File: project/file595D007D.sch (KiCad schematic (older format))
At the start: 8 parts

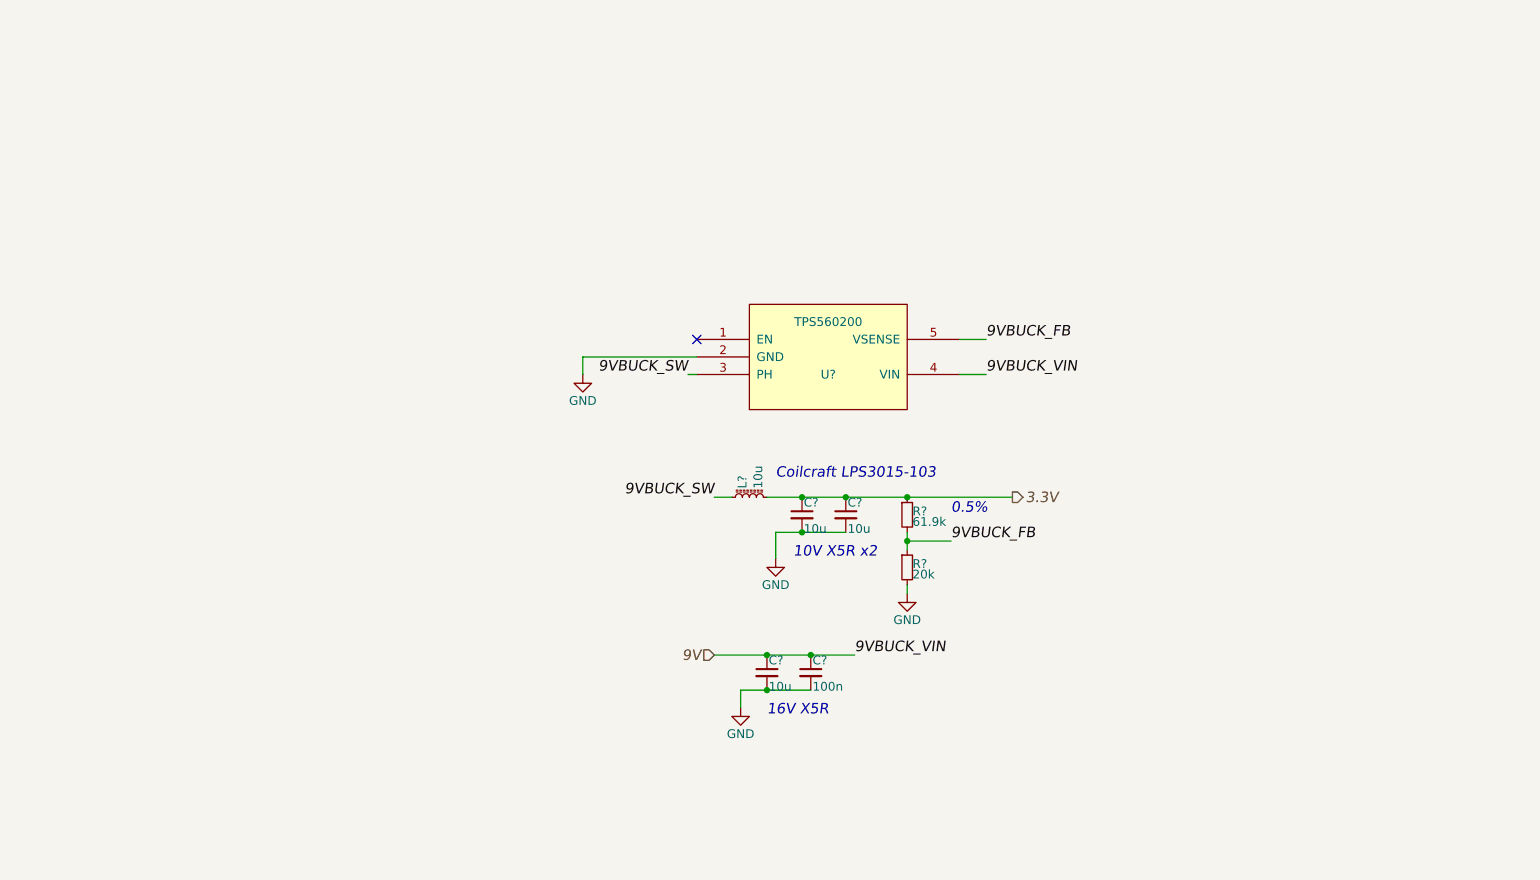
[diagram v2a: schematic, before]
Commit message: Update README with links to documentation for all parts entered in schematic so far. Add 9V to 14V boost converter for output amplifier to schematic.
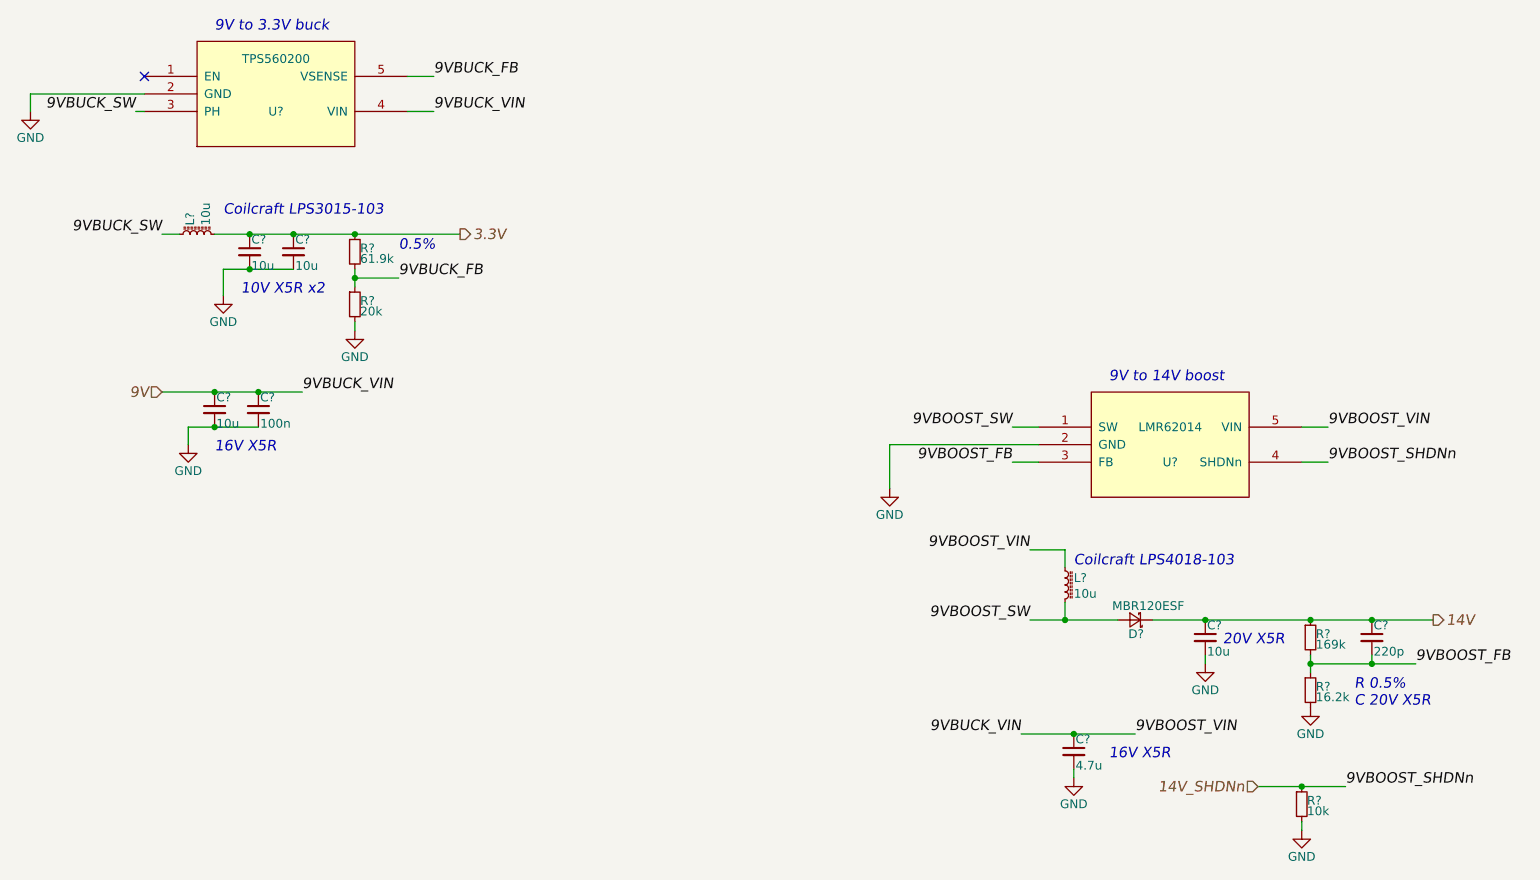
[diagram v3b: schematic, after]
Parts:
- added C?: 10u, Capacitors_SMD:C_0805, symbol C_Small
- added C?: 220p, Capacitors_SMD:C_0402, symbol C_Small
- added C?: 4.7u, Capacitors_SMD:C_0603, symbol C_Small
- added D?: MBR120ESF, Diodes_SMD:D_SOD-123F, symbol D_Schottky_Small
- added L?: 10u, symbol L_Core_Ferrite_Small
- added R?: 169k, Resistors_SMD:R_0402, symbol R_Small
- added R?: 16.2k, Resistors_SMD:R_0402, symbol R_Small
- added R?: 10k, Resistors_SMD:R_0402, symbol R_Small
- added U?: LMR62014, TO_SOT_Packages_SMD:SOT-23-5, symbol LMR62014
- U?: footprint MODULE -> TO_SOT_Packages_SMD:SOT-23-5
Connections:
- net 9V: now also C?.1, L?.1, U?.5 (VIN)
- net GND: now also C?.2, C?.2, R?.2, R?.2, U?.2 (GND)
- new net 14V: C?.1, C?.1, D?.1 (K), R?.1
- new net 14V_SHDNn: R?.1, U?.4 (SHDNn)
- new net 9VBOOST_FB: C?.2, R?.1, R?.2, U?.3 (FB)
- new net 9VBOOST_SW: D?.2 (A), L?.2, U?.1 (SW)
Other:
- note added: "20V X5R"
- note added: "9V to 14V boost"
- note added: "9V to 3.3V buck"
- note added: "Coilcraft LPS4018-103"
- note added: "R 0.5%\nC 20V X5R"
- moved on the sheet: C?, L?, R?, U?
